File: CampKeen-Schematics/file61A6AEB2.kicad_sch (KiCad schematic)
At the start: 8 parts, among them Q54 2N7000, Q55 IRF9Z34NPBF, Q56 2N7000, Q57 IRF9Z34NPBF

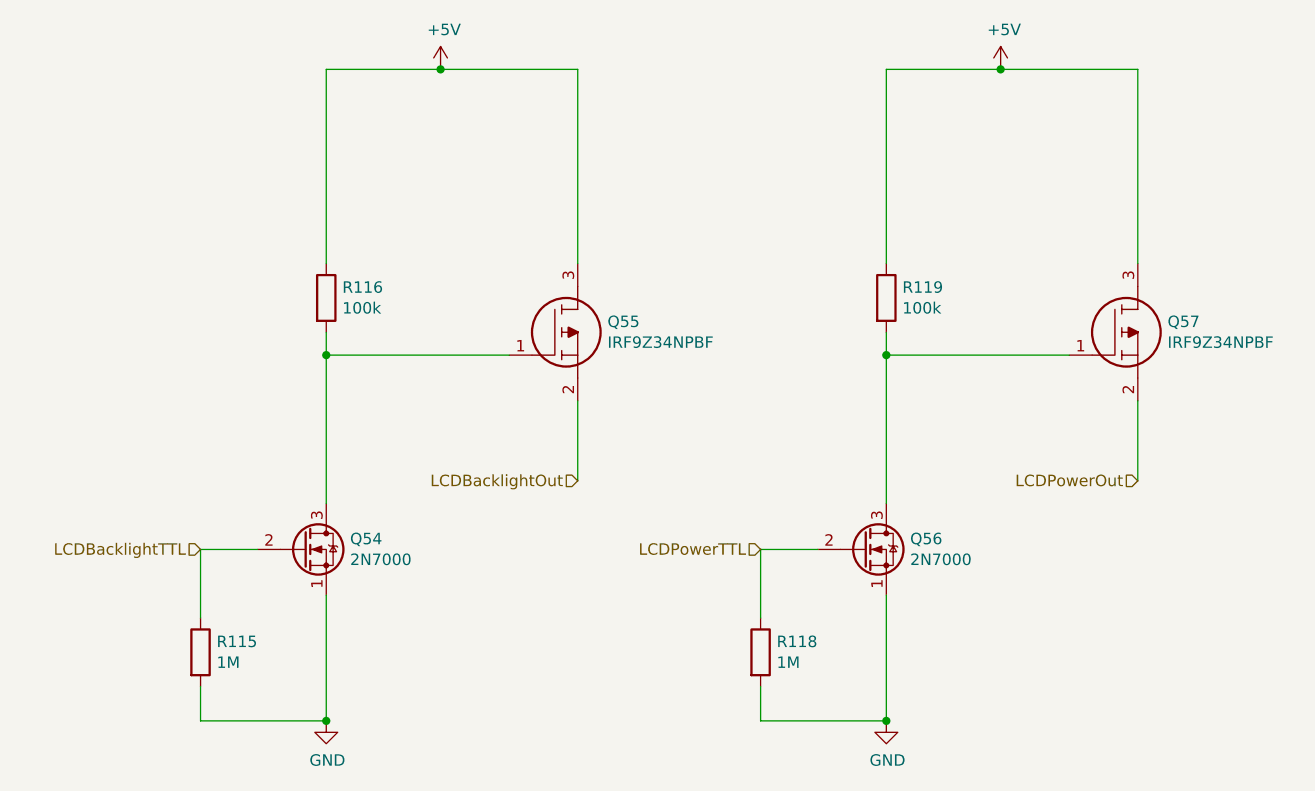
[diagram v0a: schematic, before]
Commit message: removed from schematic - lcd backlight enable - lcd backlight out - moving gpio around to get free serial pins.
starting to remove the parts from the PCB
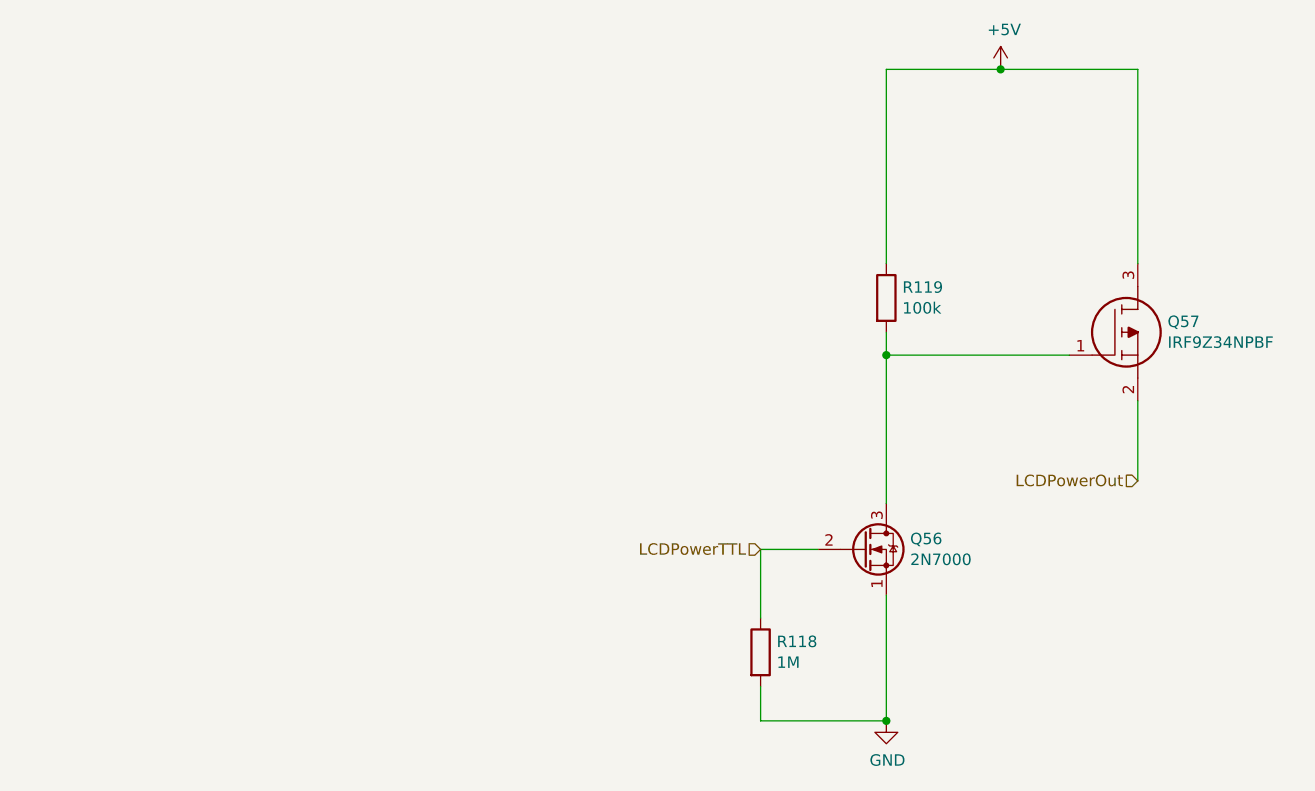
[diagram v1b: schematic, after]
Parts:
- removed Q54: 2N7000, Package_TO_SOT_THT:TO-92_Inline, symbol Transistor_FET:2N7000
- removed Q55: IRF9Z34NPBF, SamacSys_Parts:TO254P469X1042X1967-3P, symbol SamacSys_Parts:IRF9Z34NPBF
- removed R115: 1M, Resistor_THT:R_Axial_DIN0207_L6.3mm_D2.5mm_P2.54mm_Vertical, symbol Device:R
- removed R116: 100k, Resistor_THT:R_Axial_DIN0207_L6.3mm_D2.5mm_P2.54mm_Vertical, symbol Device:R
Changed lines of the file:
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@@
 (kicad_sch (version 20211123) (generator eeschema)
   (paper "A4")
-  (junction (at 149.86 85.09) (diameter 0) (color 0 0 0 0)
-  )
   (junction (at 212.09 125.73) (diameter 0) (color 0 0 0 0)
   )
@@
   )
   (junction (at 224.79 53.34) (diameter 0) (color 0 0 0 0)
-  )
-  (junction (at 149.86 125.73) (diameter 0) (color 0 0 0 0)
-  )
-  (junction (at 162.56 53.34) (diameter 0) (color 0 0 0 0)
-  )
-  (wire (pts (xy 177.8 53.34) (xy 162.56 53.34))
-    (stroke (width 0) (type default) (color 0 0 0 0))
   )
   (wire (pts (xy 212.09 111.76) (xy 212.09 125.73))
@@
     (stroke (width 0) (type default) (color 0 0 0 0))
   )
-  (wire (pts (xy 162.56 53.34) (xy 149.86 53.34))
-    (stroke (width 0) (type default) (color 0 0 0 0))
-  )
-  (wire (pts (xy 135.89 114.3) (xy 135.89 106.68))
-    (stroke (width 0) (type default) (color 0 0 0 0))
-  )
   (wire (pts (xy 198.12 121.92) (xy 198.12 125.73))
-    (stroke (width 0) (type default) (color 0 0 0 0))
-  )
-  (wire (pts (xy 149.86 53.34) (xy 149.86 74.93))
-    (stroke (width 0) (type default) (color 0 0 0 0))
-  )
-  (wire (pts (xy 135.89 125.73) (xy 149.86 125.73))
     (stroke (width 0) (type default) (color 0 0 0 0))
   )
@@
     (stroke (width 0) (type default) (color 0 0 0 0))
   )
-  (wire (pts (xy 177.8 74.93) (xy 177.8 53.34))
-    (stroke (width 0) (type default) (color 0 0 0 0))
-  )
   (wire (pts (xy 224.79 53.34) (xy 212.09 53.34))
     (stroke (width 0) (type default) (color 0 0 0 0))
   )
-  (wire (pts (xy 135.89 106.68) (xy 142.24 106.68))
-    (stroke (width 0) (type default) (color 0 0 0 0))
-  )
-  (wire (pts (xy 149.86 85.09) (xy 149.86 101.6))
-    (stroke (width 0) (type default) (color 0 0 0 0))
-  )
   (wire (pts (xy 240.03 99.06) (xy 240.03 90.17))
-    (stroke (width 0) (type default) (color 0 0 0 0))
-  )
-  (wire (pts (xy 149.86 111.76) (xy 149.86 125.73))
-    (stroke (width 0) (type default) (color 0 0 0 0))
-  )
-  (wire (pts (xy 149.86 85.09) (xy 149.86 82.55))
     (stroke (width 0) (type default) (color 0 0 0 0))
   )
@@
     (stroke (width 0) (type default) (color 0 0 0 0))
   )
-  (wire (pts (xy 149.86 85.09) (xy 170.18 85.09))
-    (stroke (width 0) (type default) (color 0 0 0 0))
-  )
-  (wire (pts (xy 177.8 99.06) (xy 177.8 90.17))
-    (stroke (width 0) (type default) (color 0 0 0 0))
-  )
   (wire (pts (xy 240.03 53.34) (xy 224.79 53.34))
     (stroke (width 0) (type default) (color 0 0 0 0))
@@
     (stroke (width 0) (type default) (color 0 0 0 0))
   )
-  (wire (pts (xy 135.89 121.92) (xy 135.89 125.73))
-    (stroke (width 0) (type default) (color 0 0 0 0))
-  )
   (wire (pts (xy 212.09 85.09) (xy 212.09 101.6))
     (stroke (width 0) (type default) (color 0 0 0 0))
   )
-  (hierarchical_label "LCDBacklightOut" (shape input) (at 177.8 99.06 180)
-    (effects (font (size 1.27 1.27)) (justify right))
-  )
   (hierarchical_label "LCDPowerTTL" (shape input) (at 198.12 106.68 180)
-    (effects (font (size 1.27 1.27)) (justify right))
-  )
-  (hierarchical_label "LCDBacklightTTL" (shape input) (at 135.89 106.68 180)
     (effects (font (size 1.27 1.27)) (justify right))
   )
@@
     (effects (font (size 1.27 1.27)) (justify right))
   )
-  (symbol (lib_id "SamacSys_Parts:IRF9Z34NPBF") (at 170.18 85.09 0) (unit 1)
-    (in_bom yes) (on_board yes)
-    (property "Reference" "Q55" (id 0) (at 181.102 81.3816 0)
-      (effects (font (size 1.27 1.27)) (justify left))
-    )
-    (property "Value" "IRF9Z34NPBF" (id 1) (at 181.102 83.693 0)
-      (effects (font (size 1.27 1.27)) (justify left))
-    )
-    (property "Footprint" "SamacSys_Parts:TO254P469X1042X1967-3P" (id 2) (at 181.61 86.36 0)
-      (effects (font (size 1.27 1.27)) (justify left) hide)
-    )
-    (property "Datasheet" "https://www.infineon.com/dgdl/irf9z34npbf.pdf?fileId=5546d462533600a40153561220af1ddd" (id 3) (at 181.61 88.9 0)
-      (effects (font (size 1.27 1.27)) (justify left) hide)
-    )
-    (property "Description" "MOSFET MOSFT PCh -55V -17A 100mOhm 23.3nC" (id 4) (at 181.61 91.44 0)
-      (effects (font (size 1.27 1.27)) (justify left) hide)
-    )
-    (property "Height" "4.69" (id 5) (at 181.61 93.98 0)
-      (effects (font (size 1.27 1.27)) (justify left) hide)
-    )
-    (property "Mouser Part Number" "942-IRF9Z34NPBF" (id 6) (at 181.61 96.52 0)
-      (effects (font (size 1.27 1.27)) (justify left) hide)
-    )
-    (property "Mouser Price/Stock" "https://www.mouser.co.uk/ProductDetail/Infineon-IR/IRF9Z34NPBF?qs=9%252BKlkBgLFf16a%2FvlD%252BMCtQ%3D%3D" (id 7) (at 181.61 99.06 0)
-      (effects (font (size 1.27 1.27)) (justify left) hide)
-    )
-    (property "Manufacturer_Name" "Infineon" (id 8) (at 181.61 101.6 0)
-      (effects (font (size 1.27 1.27)) (justify left) hide)
-    )
-    (property "Manufacturer_Part_Number" "IRF9Z34NPBF" (id 9) (at 181.61 104.14 0)
-      (effects (font (size 1.27 1.27)) (justify left) hide)
-    )
-    (pin "1")
-    (pin "2")
-    (pin "3")
-  )
-  (symbol (lib_id "Device:R") (at 135.89 118.11 0) (unit 1)
-    (in_bom yes) (on_board yes)
-    (property "Reference" "R115" (id 0) (at 137.668 116.9416 0)
-      (effects (font (size 1.27 1.27)) (justify left))
-    )
-    (property "Value" "1M" (id 1) (at 137.668 119.253 0)
-      (effects (font (size 1.27 1.27)) (justify left))
-    )
-    (property "Footprint" "Resistor_THT:R_Axial_DIN0207_L6.3mm_D2.5mm_P2.54mm_Vertical" (id 2) (at 134.112 118.11 90)
-      (effects (font (size 1.27 1.27)) hide)
-    )
-    (property "Datasheet" "~" (id 3) (at 135.89 118.11 0)
-      (effects (font (size 1.27 1.27)) hide)
-    )
-    (pin "1")
-    (pin "2")
-  )
-  (symbol (lib_id "power:GND") (at 149.86 125.73 0) (unit 1)
-    (in_bom yes) (on_board yes)
-    (property "Reference" "#PWR0149" (id 0) (at 149.86 132.08 0)
-      (effects (font (size 1.27 1.27)) hide)
-    )
-    (property "Value" "GND" (id 1) (at 149.987 130.1242 0))
-    (property "Footprint" "" (id 2) (at 149.86 125.73 0)
-      (effects (font (size 1.27 1.27)) hide)
-    )
-    (property "Datasheet" "" (id 3) (at 149.86 125.73 0)
-      (effects (font (size 1.27 1.27)) hide)
-    )
-    (pin "1")
-  )
-  (symbol (lib_id "Transistor_FET:2N7000") (at 147.32 106.68 0) (unit 1)
-    (in_bom yes) (on_board yes)
-    (property "Reference" "Q54" (id 0) (at 152.5016 105.5116 0)
-      (effects (font (size 1.27 1.27)) (justify left))
-    )
-    (property "Value" "2N7000" (id 1) (at 152.5016 107.823 0)
-      (effects (font (size 1.27 1.27)) (justify left))
-    )
-    (property "Footprint" "Package_TO_SOT_THT:TO-92_Inline" (id 2) (at 152.4 108.585 0)
-      (effects (font (size 1.27 1.27) italic) (justify left) hide)
-    )
-    (property "Datasheet" "https://www.onsemi.com/pub/Collateral/NDS7002A-D.PDF" (id 3) (at 147.32 106.68 0)
-      (effects (font (size 1.27 1.27)) (justify left) hide)
-    )
-    (pin "1")
-    (pin "2")
-    (pin "3")
-  )
-  (symbol (lib_id "Device:R") (at 149.86 78.74 0) (unit 1)
-    (in_bom yes) (on_board yes)
-    (property "Reference" "R116" (id 0) (at 151.638 77.5716 0)
-      (effects (font (size 1.27 1.27)) (justify left))
-    )
-    (property "Value" "100k" (id 1) (at 151.638 79.883 0)
-      (effects (font (size 1.27 1.27)) (justify left))
-    )
-    (property "Footprint" "Resistor_THT:R_Axial_DIN0207_L6.3mm_D2.5mm_P2.54mm_Vertical" (id 2) (at 148.082 78.74 90)
-      (effects (font (size 1.27 1.27)) hide)
-    )
-    (property "Datasheet" "~" (id 3) (at 149.86 78.74 0)
-      (effects (font (size 1.27 1.27)) hide)
-    )
-    (pin "1")
-    (pin "2")
-  )
-  (symbol (lib_id "power:+5V") (at 162.56 53.34 0) (unit 1)
-    (in_bom yes) (on_board yes)
-    (property "Reference" "#PWR0150" (id 0) (at 162.56 57.15 0)
-      (effects (font (size 1.27 1.27)) hide)
-    )
-    (property "Value" "+5V" (id 1) (at 162.941 48.9458 0))
-    (property "Footprint" "" (id 2) (at 162.56 53.34 0)
-      (effects (font (size 1.27 1.27)) hide)
-    )
-    (property "Datasheet" "" (id 3) (at 162.56 53.34 0)
-      (effects (font (size 1.27 1.27)) hide)
-    )
-    (pin "1")
-  )
   (symbol (lib_id "SamacSys_Parts:IRF9Z34NPBF") (at 232.41 85.09 0) (unit 1)

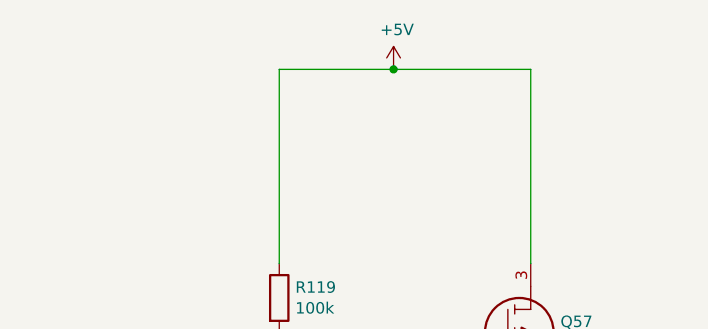
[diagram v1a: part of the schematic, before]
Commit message: cleaned up the PCB changes by removing the old traces and vias from pin swaps got the ESP socket grouped and space correctly need to move some things around to get it onto the board.
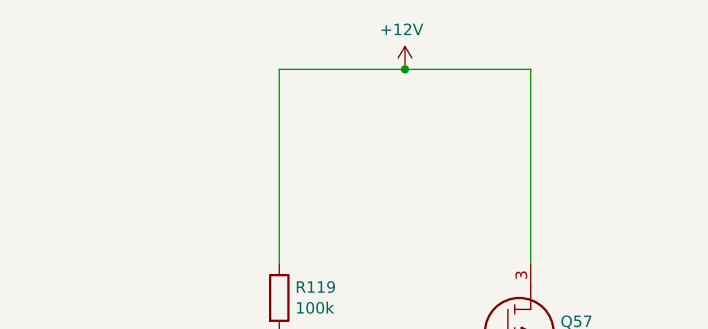
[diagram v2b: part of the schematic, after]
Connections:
- net +5V renamed +12V
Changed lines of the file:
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@@
   (junction (at 212.09 85.09) (diameter 0) (color 0 0 0 0)
   )
-  (junction (at 224.79 53.34) (diameter 0) (color 0 0 0 0)
+  (junction (at 226.06 53.34) (diameter 0) (color 0 0 0 0)
   )
   (wire (pts (xy 212.09 111.76) (xy 212.09 125.73))
@@
     (stroke (width 0) (type default) (color 0 0 0 0))
   )
+  (wire (pts (xy 226.06 53.34) (xy 240.03 53.34))
+    (stroke (width 0) (type default) (color 0 0 0 0))
+  )
   (wire (pts (xy 212.09 85.09) (xy 232.41 85.09))
     (stroke (width 0) (type default) (color 0 0 0 0))
   )
-  (wire (pts (xy 224.79 53.34) (xy 212.09 53.34))
+  (wire (pts (xy 212.09 53.34) (xy 226.06 53.34))
     (stroke (width 0) (type default) (color 0 0 0 0))
   )
@@
   )
   (wire (pts (xy 212.09 85.09) (xy 212.09 82.55))
-    (stroke (width 0) (type default) (color 0 0 0 0))
-  )
-  (wire (pts (xy 240.03 53.34) (xy 224.79 53.34))
     (stroke (width 0) (type default) (color 0 0 0 0))
   )
@@
     (pin "2")
   )
-  (symbol (lib_id "power:+5V") (at 224.79 53.34 0) (unit 1)
+  (symbol (lib_id "power:+12V") (at 226.06 53.34 0) (mirror y) (unit 1)
     (in_bom yes) (on_board yes)
-    (property "Reference" "#PWR0152" (id 0) (at 224.79 57.15 0)
+    (property "Reference" "#PWR?" (id 0) (at 226.06 57.15 0)
       (effects (font (size 1.27 1.27)) hide)
     )
-    (property "Value" "+5V" (id 1) (at 225.171 48.9458 0))
-    (property "Footprint" "" (id 2) (at 224.79 53.34 0)
+    (property "Value" "+12V" (id 1) (at 225.679 48.9458 0))
+    (property "Footprint" "" (id 2) (at 226.06 53.34 0)
       (effects (font (size 1.27 1.27)) hide)
     )
-    (property "Datasheet" "" (id 3) (at 224.79 53.34 0)
+    (property "Datasheet" "" (id 3) (at 226.06 53.34 0)
       (effects (font (size 1.27 1.27)) hide)
     )

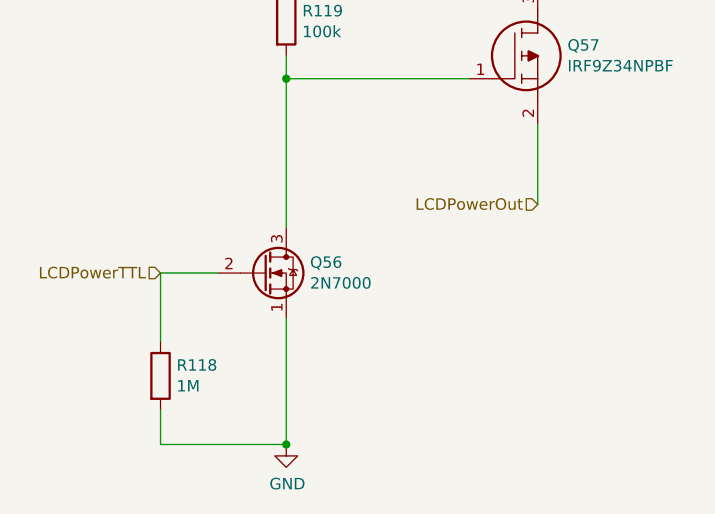
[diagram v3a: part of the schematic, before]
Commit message: alright massive changes. some part switches and some reassignments. mostly it's switching out stuff for SMD so that i have more space.
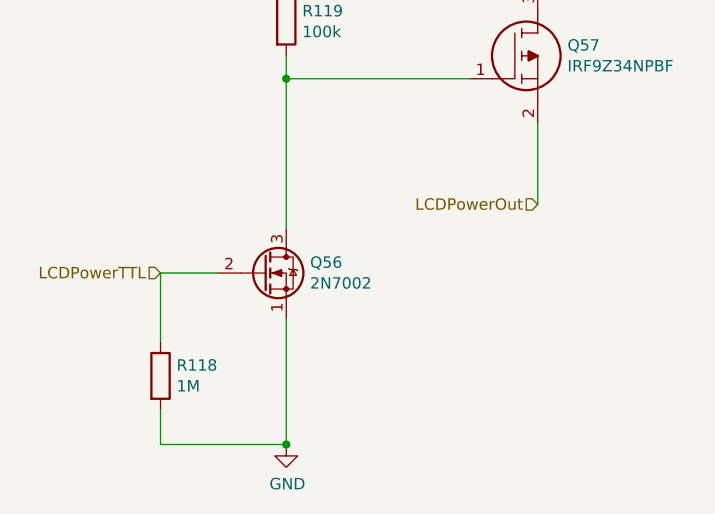
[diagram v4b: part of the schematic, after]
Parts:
- Q56: value 2N7000 -> 2N7002; footprint Package_TO_SOT_THT:TO-92_Inline -> Package_TO_SOT_SMD:SOT-23
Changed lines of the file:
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@@
       (effects (font (size 1.27 1.27)) (justify left))
     )
-    (property "Value" "2N7000" (id 1) (at 214.7316 107.823 0)
+    (property "Value" "2N7002" (id 1) (at 214.7316 107.823 0)
       (effects (font (size 1.27 1.27)) (justify left))
     )
-    (property "Footprint" "Package_TO_SOT_THT:TO-92_Inline" (id 2) (at 214.63 108.585 0)
+    (property "Footprint" "Package_TO_SOT_SMD:SOT-23" (id 2) (at 214.63 108.585 0)
       (effects (font (size 1.27 1.27) italic) (justify left) hide)
     )
